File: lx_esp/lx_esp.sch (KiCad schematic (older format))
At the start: 27 parts, among them J1 Conn_01x02, J2 200LX_02X05, Q1 Dual_Nch_MOSFET, SW1 SW_Push, SW2 SW_Push, U1 LTC4365, U2 XC6210, U3 ESP-12F, U4 TRS3238E

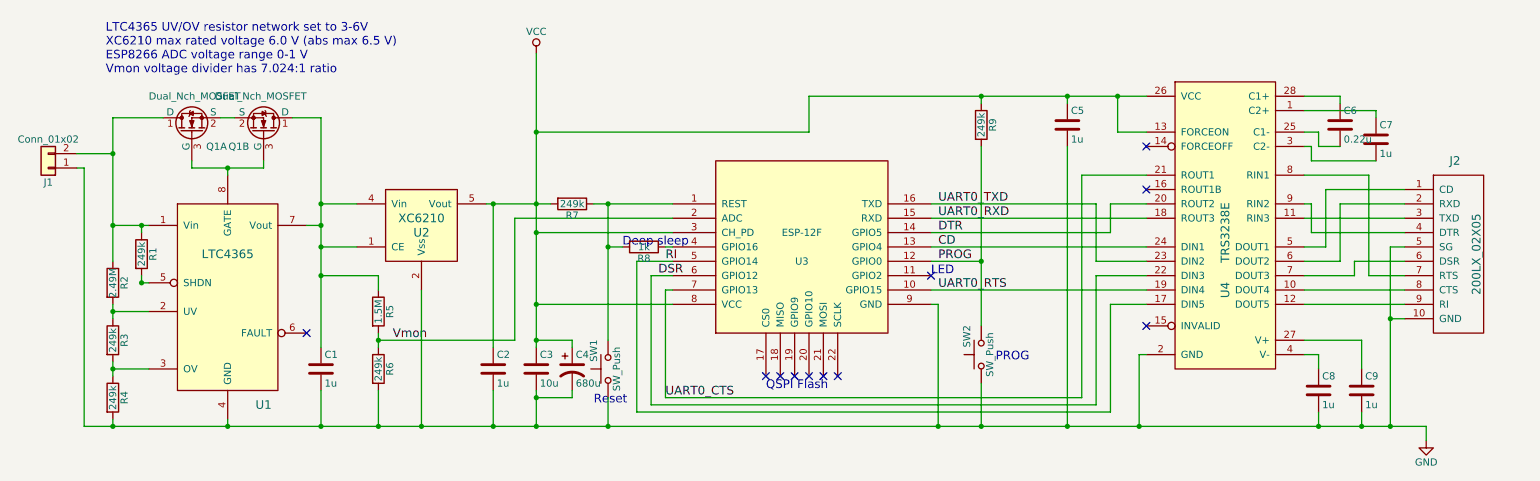
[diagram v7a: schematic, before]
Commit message: footprints for switches
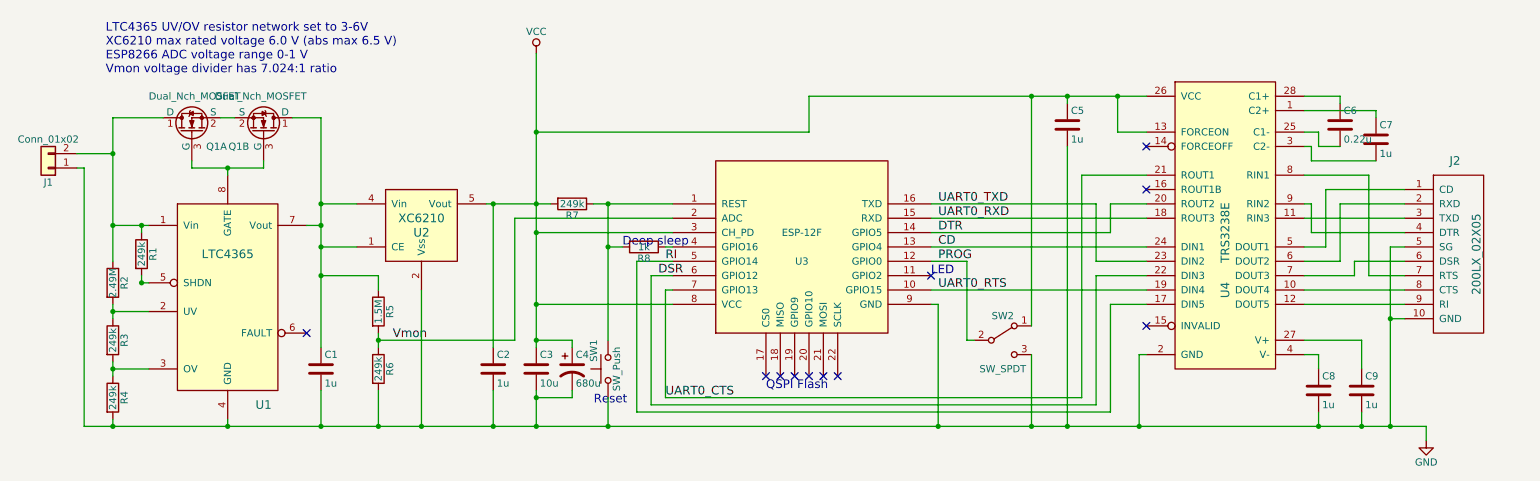
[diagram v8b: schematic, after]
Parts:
- removed R9: 249k, Resistors_SMD:R_0805_HandSoldering, symbol R
- removed SW2: SW_Push, symbol SW_Push
- added SW2: SW_SPDT, ssop_20:CL-SB-12B-02T, symbol SW_SPDT
- J1: footprint Pin_Headers:Pin_Header_Straight_1x02_Pitch2.54mm -> Connectors_JST:JST_PH_S2B-PH-K_02x2.00mm_Angled
- SW1: footprint (none) -> ssop_20:TL3305
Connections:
- net GND: now also SW2.3 (C)
- net PROG: now also SW2.2 (B)
- net VCC: now also SW2.1 (A)
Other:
- note removed: "PROG"
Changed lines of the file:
@@
 F 0 "SW1" H 4650 4500 50  0000 L CNN
 F 1 "SW_Push" H 4600 4340 50  0000 C CNN
-F 2 "" H 4600 4600 50  0001 C CNN
+F 2 "ssop_20:TL3305" H 4600 4600 50  0001 C CNN
 F 3 "" H 4600 4600 50  0001 C CNN
 	1    4600 4400
@@
 F 0 "J1" H 700 3100 50  0000 C CNN
 F 1 "Conn_01x02" H 700 2800 50  0000 C CNN
-F 2 "Pin_Headers:Pin_Header_Straight_1x02_Pitch2.54mm" H 700 3000 50  0001 C CNN
+F 2 "Connectors_JST:JST_PH_S2B-PH-K_02x2.00mm_Angled" H 700 3000 50  0001 C CNN
 F 3 "" H 700 3000 50  0001 C CNN
 	1    700  3000
@@
 	1    0    0    -1
 $EndComp
-$Comp
-L SW_Push SW2
-U 1 1 5A92436B
-P 7200 4300
-F 0 "SW2" H 7250 4400 50  0000 L CNN
-F 1 "SW_Push" H 7200 4240 50  0000 C CNN
-F 2 "" H 7200 4500 50  0001 C CNN
-F 3 "" H 7200 4500 50  0001 C CNN
-	1    7200 4300
-	0    -1   -1   0
-$EndComp
 NoConn ~ 6850 3750
-$Comp
-L R R9
-U 1 1 5A924548
-P 7200 2700
-F 0 "R9" V 7280 2700 50  0000 C CNN
-F 1 "249k" V 7200 2700 50  0000 C CNN
-F 2 "Resistors_SMD:R_0805_HandSoldering" V 7130 2700 50  0001 C CNN
-F 3 "" H 7200 2700 50  0001 C CNN
-	1    7200 2700
-	1    0    0    -1
-$EndComp
-Text Notes 7300 4350 0    60   ~ 0
-PROG
 $Comp
 L VCC #PWR02
@@
 	6850 3950 6900 3950
 Wire Wire Line
-	6900 3950 6900 4800
+	6900 4800 6900 3950
 Wire Wire Line
 	5050 3850 5000 3850
@@
 	6000 2500 8350 2500
 Wire Wire Line
-	6850 3650 7200 3650
-Wire Wire Line
-	7200 2850 7200 4100
-Connection ~ 7200 3650
-Wire Wire Line
-	7200 2550 7200 2500
-Wire Wire Line
-	7200 4800 7200 4500
-Connection ~ 7200 4800
-Wire Wire Line
 	3950 3350 3950 4200
 Wire Wire Line
@@
 	3000 3850 3000 3750
 Wire Wire Line
-	3000 3750 2600 3750
+	2600 3750 3000 3750
 Connection ~ 2600 3750
 Wire Wire Line
@@
 Wire Wire Line
 	6000 2750 6000 2500
-Connection ~ 7200 2500
 Connection ~ 4100 2750
 Wire Wire Line
@@
 	3300 3850 3300 4800
 Connection ~ 3300 4800
-Text Label 6900 3650 0    60   ~ 0
-PROG
 Text Notes 1100 2350 0    60   ~ 0
 LTC4365 UV/OV resistor network set to 3-6V\nXC6210 max rated voltage 6.0 V (abs max 6.5 V)\nESP8266 ADC voltage range 0-1 V\nVmon voltage divider has 7.024:1 ratio
 Text Label 3100 4200 0    60   ~ 0
 Vmon
+$Comp
+L SW_SPDT SW2
+U 1 1 5AA19D0E
+P 7350 4200
+F 0 "SW2" H 7350 4370 50  0000 C CNN
+F 1 "SW_SPDT" H 7350 4000 50  0000 C CNN
+F 2 "ssop_20:CL-SB-12B-02T" H 7350 4200 50  0001 C CNN
+F 3 "" H 7350 4200 50  0001 C CNN
+	1    7350 4200
+	1    0    0    -1
+$EndComp
+Wire Wire Line
+	7550 4100 7550 2500
+Connection ~ 7550 2500
+Wire Wire Line
+	7550 4300 7550 4800
+Connection ~ 7550 4800
+Wire Wire Line
+	6850 3650 7100 3650
+Wire Wire Line
+	7100 3650 7100 4200
+Wire Wire Line
+	7100 4200 7150 4200
+Text Label 6900 3650 0    60   ~ 0
+PROG
 $EndSCHEMATC
